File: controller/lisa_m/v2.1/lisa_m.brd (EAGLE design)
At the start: 50.7 x 33.6 mm, 119 parts, among them IC9 LP2992 5V, J1 CONN_3-1, J2 CONN_3-1, J3 CONN_3-1, J4 CONN_3-1, J5 CONN_3-1, J6 CONN_3-1, J7 CONN_3-1, J8 CONN_3-1, Q1 12Mhz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

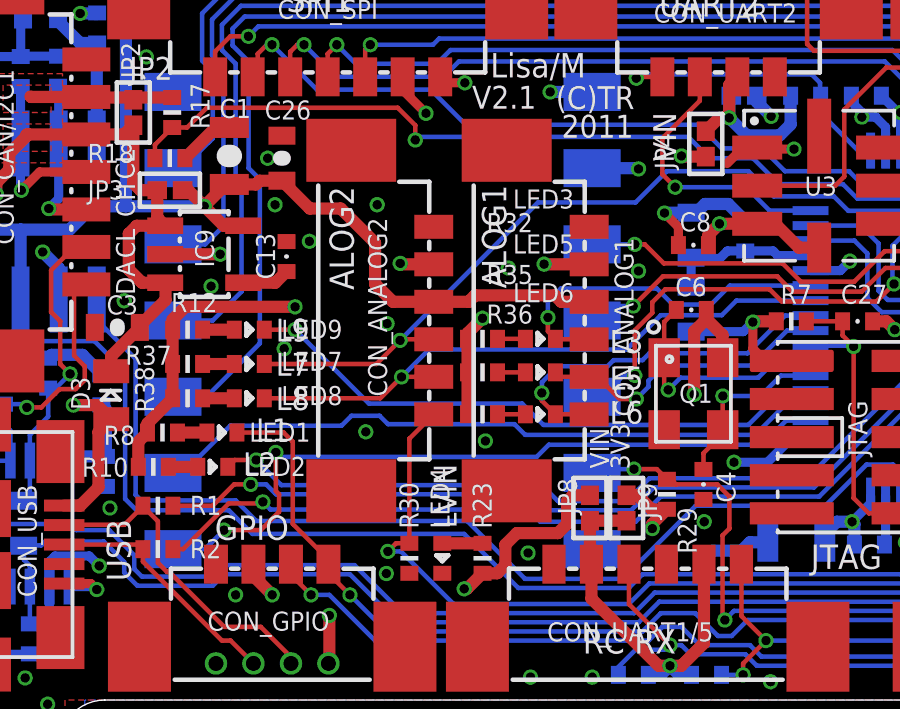
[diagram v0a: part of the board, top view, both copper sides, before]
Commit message: changed LED labeling to be more intuitive for a user, both on schematic and on silkscreens, also changed power led schematic name to LEDVIN to keep better consistency with silkscreen and remove number since it can't be controlled
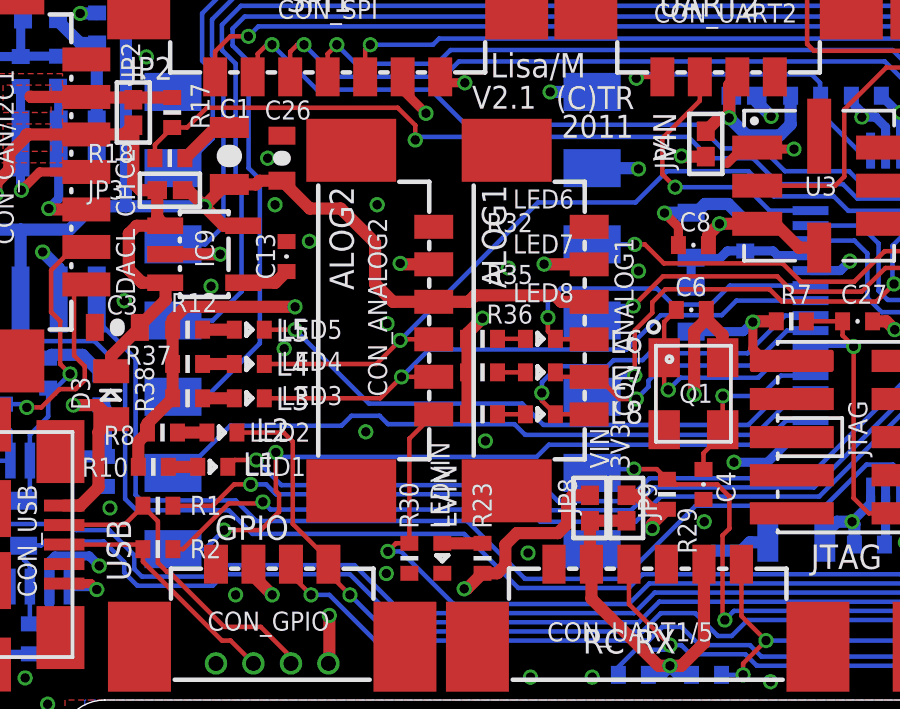
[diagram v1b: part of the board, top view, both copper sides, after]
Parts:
- removed LED9: BLU, pel_dipol_comp:0402-LED
- added LEDVIN: ORG, pel_dipol_comp:0402-LED
- LED1: value RED -> BLU
- LED2: value BLU -> RED
- LED4: value ORG -> BLU
- moved LED3 9.90 mm to (10.5, 10.1)
- moved LED5 9.81 mm to (10.5, 12.3)
- moved LED8 9.72 mm to (20.2, 9.53)
- moved LED7 9.71 mm to (20.2, 10.9)
- moved LED4 9.13 mm to (10.5, 11.2), turned to 0 degrees
- moved LED6 2.51 mm to (20.2, 12.0)
- moved LED1 1.18 mm to (9.30, 7.77)
- moved LED2 1.18 mm to (9.60, 8.92)
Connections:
- net ADC_1: now also LED6.C; no longer LED3.C
- net ADC_2: now also LED7.C; no longer LED5.C
- net ADC_3: now also LED8.C; no longer LED6.C
- net ADC_4: now also LED4.C; no longer LED7.C
- net ADC_6: now also LED3.C; no longer LED8.C
- net GND: now also LEDVIN.C; no longer LED4.C
- net JTAG_TRST: now also LED2.C; no longer LED1.C
- net LED1: now also LED1.C; no longer LED2.C
- net LED2: now also LED5.C; no longer LED9.C
- net N$10: now also LED2.A; no longer LED1.A
- net N$11: now also LED8.A; no longer LED6.A
- net N$12: now also LEDVIN.A; no longer LED4.A
- net N$13: now also LED5.A; no longer LED9.A
- net N$14: now also LED4.A; no longer LED7.A
- net N$15: now also LED3.A; no longer LED8.A
- net N$4: now also LED1.A; no longer LED2.A
- net N$5: now also LED6.A; no longer LED3.A
- net N$9: now also LED7.A; no longer LED5.A
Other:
- board text added: "L4"
- board text removed: "L9"
